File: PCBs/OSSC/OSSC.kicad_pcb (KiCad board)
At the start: 2 copper layers, 6 parts, among them J1 Conn_01x02_Female, U1 MCP1700-3302E_SOT23, U2 ESP32-WROOM-32, U3 MPU-6050

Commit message: Add files via upload
NEW KICAD PCB-Layout
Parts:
- moved C1 5.24 mm to (69.8, 82.5), turned to 90 degrees
- moved C2 1.41 mm to (75.1, 76.2)
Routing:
- net GND: track 72.8 -> 28.8 mm, vias 4 -> 6
- net /3.3V: track 43.9 -> 57.4 mm, vias 3 -> 0
- net +BATT: track 0.00 -> 5.08 mm
- net Net-(C1-Pad1): track 7.36 -> 2.61 mm
- net Net-(U2-Pad36): track 40.6 -> 38.0 mm
- net Net-(U2-Pad23): track 18.5 -> 16.3 mm
- net Net-(U2-Pad33): track 31.9 -> 30.7 mm
- added copper zone on B.Cu, net GND

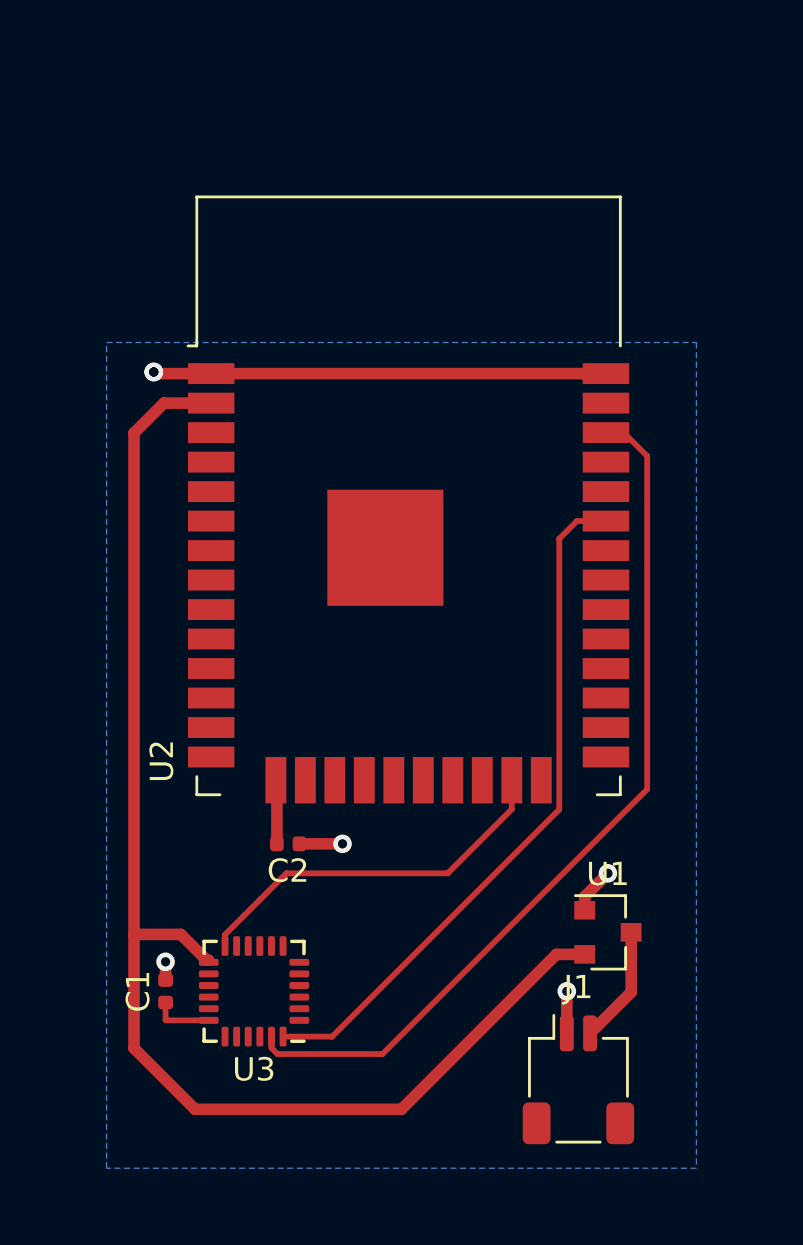
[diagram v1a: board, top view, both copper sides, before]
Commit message: Schematic Change
-Removed 2 Cap between IC-Ground to Ground
-Added Power-Up Delay-Circuit for ESP
-Added Filter-Cap for MPU
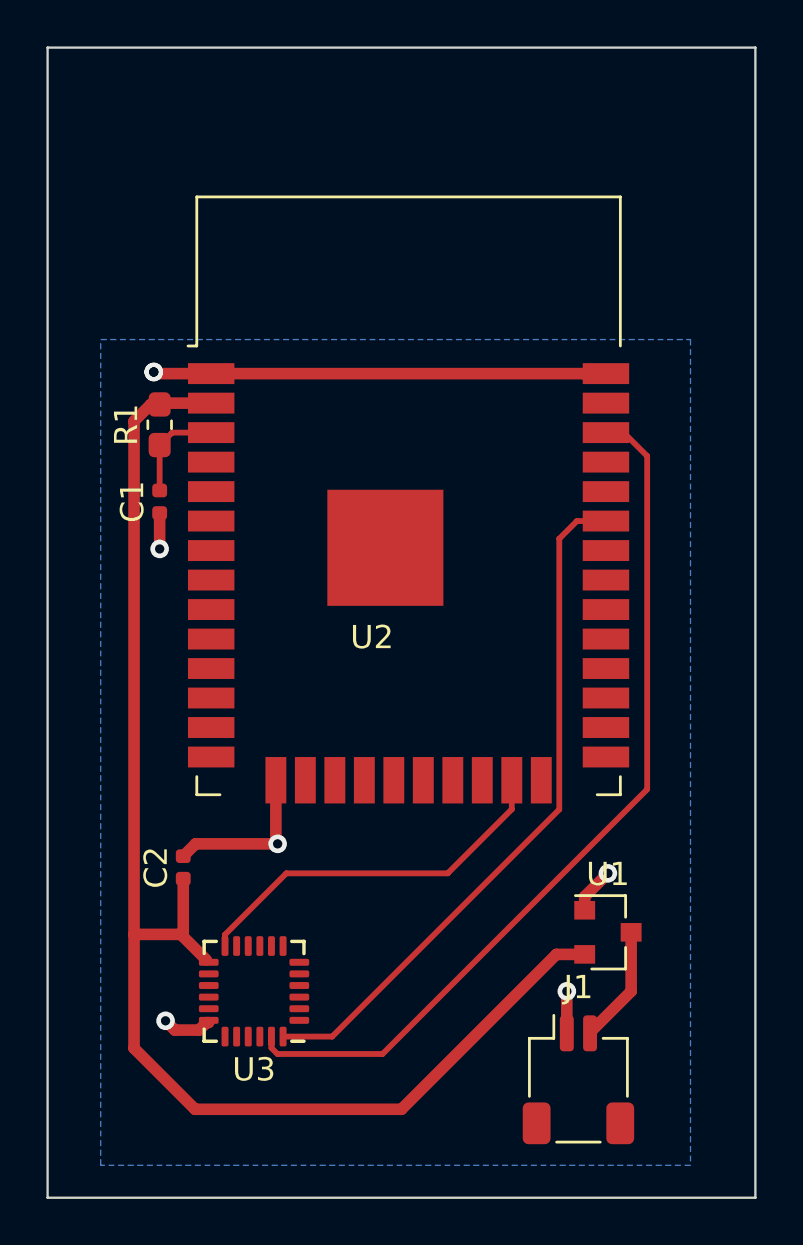
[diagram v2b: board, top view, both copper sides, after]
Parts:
- added R1: 10k, Resistor_SMD:R_0603_1608Metric_Pad1.05x0.95mm_HandSolder, F.Cu at (69.6, 58.2)
- C1, C2: value C -> 0.1mu
- moved C1 21.1 mm to (69.6, 61.5)
- moved C2 4.63 mm to (70.6, 77.2), turned to 90 degrees
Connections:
- C1 pad 1: Net-(C1-Pad1) -> GND
- C1 pad 2: GND -> Net-(C1-Pad2)
- C2 pad 1: GND -> /3.3V
- U2 pad 10: Net-(U2-Pad10) -> (no net)
- U2 pad 11: Net-(U2-Pad11) -> (no net)
- U2 pad 12: Net-(U2-Pad12) -> (no net)
- U2 pad 13: Net-(U2-Pad13) -> (no net)
- U2 pad 14: Net-(U2-Pad14) -> (no net)
- U2 pad 16: Net-(U2-Pad16) -> (no net)
- U2 pad 17: Net-(U2-Pad17) -> (no net)
- U2 pad 18: Net-(U2-Pad18) -> (no net)
- U2 pad 19: Net-(U2-Pad19) -> (no net)
- U2 pad 20: Net-(U2-Pad20) -> (no net)
- U2 pad 21: Net-(U2-Pad21) -> (no net)
- U2 pad 22: Net-(U2-Pad22) -> (no net)
- U2 pad 24: Net-(U2-Pad24) -> (no net)
- U2 pad 25: Net-(U2-Pad25) -> (no net)
- U2 pad 26: Net-(U2-Pad26) -> (no net)
- U2 pad 27: Net-(U2-Pad27) -> (no net)
- U2 pad 28: Net-(U2-Pad28) -> (no net)
- U2 pad 29: Net-(U2-Pad29) -> (no net)
- U2 pad 3: Net-(U2-Pad3) -> Net-(C1-Pad2)
- U2 pad 30: Net-(U2-Pad30) -> (no net)
- U2 pad 31: Net-(U2-Pad31) -> (no net)
- U2 pad 32: Net-(U2-Pad32) -> (no net)
- U2 pad 34: Net-(U2-Pad34) -> (no net)
- U2 pad 35: Net-(U2-Pad35) -> (no net)
- U2 pad 37: Net-(U2-Pad37) -> (no net)
- U2 pad 39: Net-(C2-Pad1) -> GND
- U2 pad 4: Net-(U2-Pad4) -> (no net)
- U2 pad 5: Net-(U2-Pad5) -> (no net)
- U2 pad 6: Net-(U2-Pad6) -> (no net)
- U2 pad 7: Net-(U2-Pad7) -> (no net)
- U2 pad 8: Net-(U2-Pad8) -> (no net)
- U2 pad 9: Net-(U2-Pad9) -> (no net)
- U3 pad 1: Net-(U3-Pad1) -> (no net)
- U3 pad 10: Net-(U3-Pad10) -> (no net)
- U3 pad 11: Net-(U3-Pad11) -> (no net)
- U3 pad 18: Net-(C1-Pad1) -> GND
- U3 pad 20: Net-(U3-Pad20) -> (no net)
- U3 pad 6: Net-(U3-Pad6) -> (no net)
- U3 pad 7: Net-(U3-Pad7) -> (no net)
- U3 pad 8: Net-(U3-Pad8) -> (no net)
- U3 pad 9: Net-(U3-Pad9) -> (no net)
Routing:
- net GND: track 28.8 -> 34.2 mm, vias 6 -> 7
- net Net-(C1-Pad2): track 0.00 -> 4.40 mm
- net /3.3V: track 57.4 -> 60.0 mm
- net Net-(C1-Pad1): track 2.61 -> 0.00 mm
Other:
- board outline added: 30.5 x 49.5 mm

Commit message: Added Components
Added Components for MPU-6050
Added I2C-Connector for Display
Added two Pins for Programming
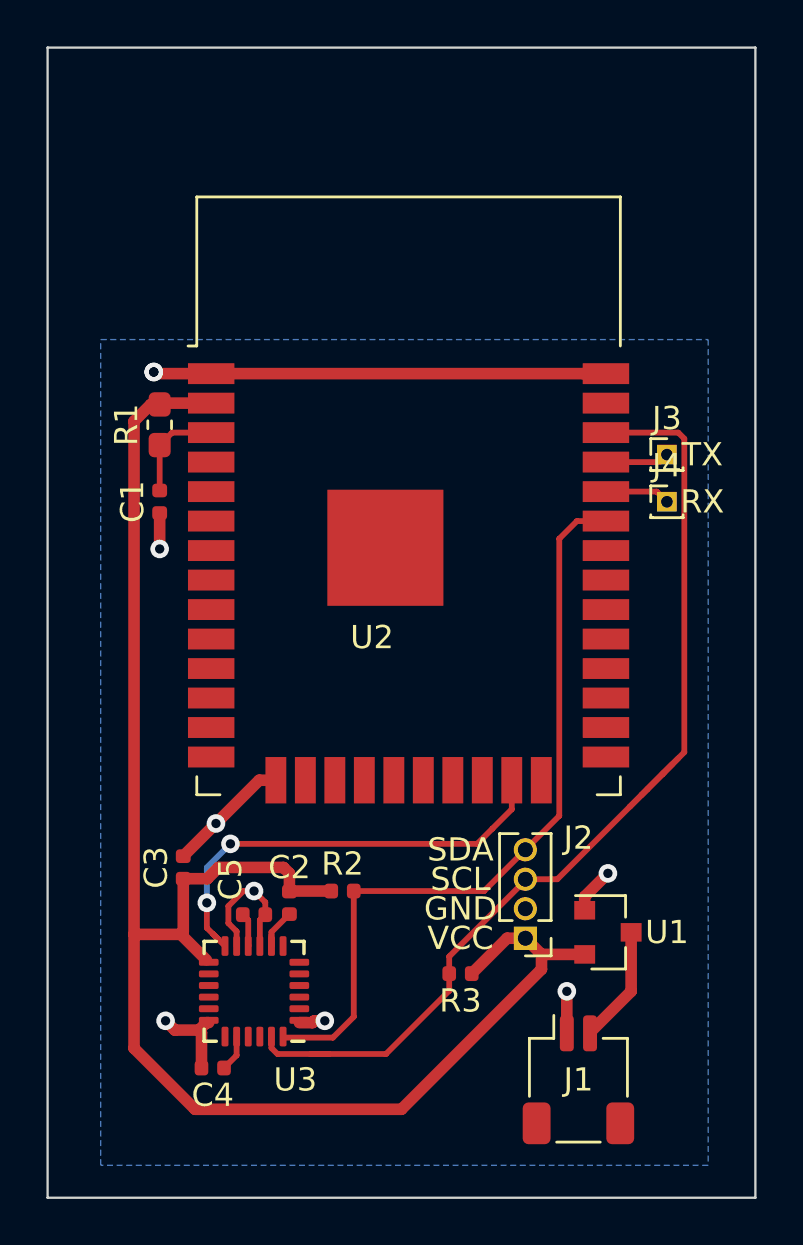
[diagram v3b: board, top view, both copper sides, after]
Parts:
- added C2: 2.2nF, Capacitor_SMD:C_0402_1005Metric, F.Cu at (75.2, 78.7)
- added C4: 2.3nF, Capacitor_SMD:C_0402_1005Metric, F.Cu at (71.9, 85.9)
- added C5: 0.1uF, Capacitor_SMD:C_0402_1005Metric, F.Cu at (73.7, 79.2)
- added J2: Conn_01x04, Connector_PinHeader_1.27mm:PinHeader_1x04_P1.27mm_Vertical, F.Cu at (85.3, 80.3)
- added J3: Conn_01x01, Connector_PinHeader_1.00mm:PinHeader_1x01_P1.00mm_Vertical, F.Cu at (91.4, 59.4)
- added J4: Conn_01x01, Connector_PinHeader_1.00mm:PinHeader_1x01_P1.00mm_Vertical, F.Cu at (91.4, 61.5)
- added R2: 10k, Resistor_SMD:R_0402_1005Metric, F.Cu at (77.5, 78.2)
- added R3: 10k, Resistor_SMD:R_0402_1005Metric, F.Cu at (82.5, 81.8)
- C1: value 0.1mu -> 0.1uF
- C3: renamed from C2; value 0.1mu -> 0.1uF
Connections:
- net /3.3V renamed VCC-3.3V
- net Net-(U2-Pad23) renamed MPU-6050-INT
- net Net-(U2-Pad33) renamed I2C-SDA
- net Net-(U2-Pad36) renamed I2C-SCL
- U2 pad 34: (no net) -> Net-(J4-Pad1)
- U2 pad 35: (no net) -> Net-(J3-Pad1)
- U3 pad 1: (no net) -> GND
- U3 pad 10: (no net) -> Net-(C5-Pad2)
- U3 pad 11: (no net) -> GND
- U3 pad 20: (no net) -> Net-(C4-Pad1)
- U3 pad 8: (no net) -> Net-(C2-Pad1)
- U3 pad 9: (no net) -> GND
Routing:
- net VCC-3.3V: track 60.0 -> 71.8 mm
- net I2C-SCL: track 38.0 -> 48.1 mm
- net GND: track 34.2 -> 41.2 mm, vias 7 -> 9
- net I2C-SDA: track 30.7 -> 34.1 mm
- net MPU-6050-INT: track 16.3 -> 19.4 mm, vias 0 -> 2
- net Net-(J3-Pad1): track 0.00 -> 2.86 mm
- net Net-(J4-Pad1): track 0.00 -> 2.81 mm
- net Net-(C2-Pad1): track 0.00 -> 2.19 mm
- net Net-(C4-Pad1): track 0.00 -> 1.58 mm
- net Net-(C5-Pad2): track 0.00 -> 1.48 mm
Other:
- board text added: "GND"
- board text added: "RX"
- board text added: "SCL"
- board text added: "SDA"
- board text added: "TX"
- board text added: "VCC"
